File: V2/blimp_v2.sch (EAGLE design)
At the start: 10 parts

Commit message: upload the finished routing pcb design
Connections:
- net GND: no longer U$2.GND, U$2.GND3, U$4.GND, U$4.GND3
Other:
- moved on the sheet: JP1, JP2, JP3, JP4, JP5, JP6, JP7

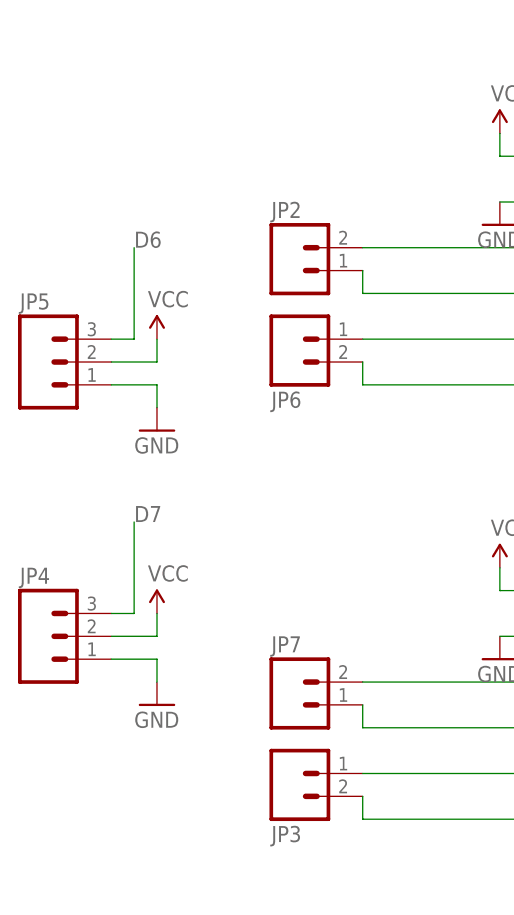
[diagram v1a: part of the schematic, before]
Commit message: add one more servo motor pinout
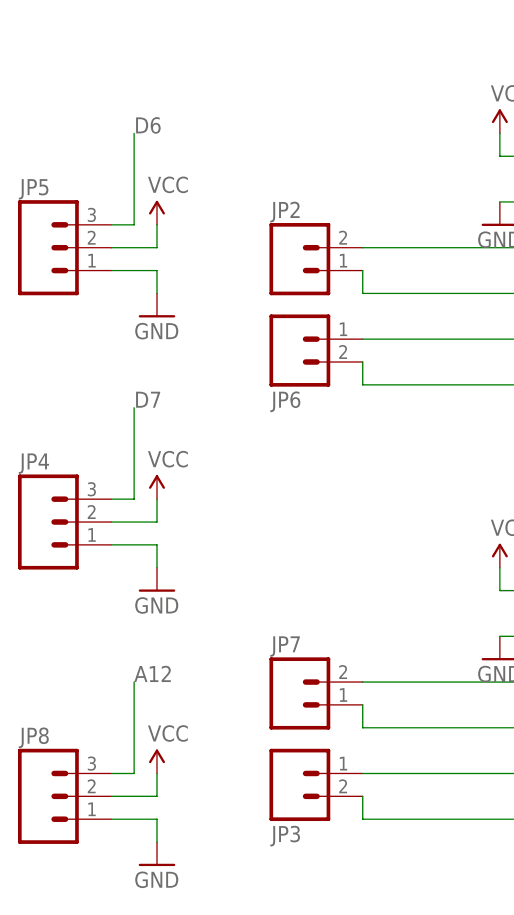
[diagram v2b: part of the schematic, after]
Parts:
- added JP8: (no value), SparkFun:M03PTH
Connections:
- net A12: now also JP8.3
- net GND: now also JP8.1
- net VCC: now also JP8.2
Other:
- moved on the sheet: JP4, JP5
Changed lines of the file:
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@@
 <part name="JP7" library="SparkFun" deviceset="M02" device="PTH"/>
 <part name="FRAME1" library="SparkFun-Aesthetics" library_urn="urn:adsk.eagle:library:507" deviceset="FRAME-A4L" device=""/>
+<part name="JP8" library="SparkFun" deviceset="M03" device="PTH"/>
+<part name="P+8" library="SparkFun" deviceset="VCC" device=""/>
+<part name="GND6" library="SparkFun" deviceset="GND" device=""/>
 </parts>
 <sheets>
@@
 <attribute name="NAME" x="-129.54" y="-41.402" size="1.778" layer="95" rot="MR180"/>
 </instance>
-<instance part="JP4" gate="G$1" x="-154.94" y="-20.32" smashed="yes">
-<attribute name="VALUE" x="-157.48" y="-27.94" size="1.778" layer="96"/>
-<attribute name="NAME" x="-157.48" y="-14.478" size="1.778" layer="95"/>
+<instance part="JP4" gate="G$1" x="-154.94" y="-7.62" smashed="yes">
+<attribute name="VALUE" x="-157.48" y="-15.24" size="1.778" layer="96"/>
+<attribute name="NAME" x="-157.48" y="-1.778" size="1.778" layer="95"/>
 </instance>
 <instance part="GND1" gate="1" x="35.56" y="7.62" smashed="yes">
@@
 <attribute name="VALUE" x="-106.68" y="-25.4" size="1.778" layer="96"/>
 </instance>
-<instance part="GND5" gate="1" x="-142.24" y="-27.94" smashed="yes">
-<attribute name="VALUE" x="-144.78" y="-30.48" size="1.778" layer="96"/>
-</instance>
-<instance part="P+4" gate="1" x="-142.24" y="-17.78" smashed="yes">
-<attribute name="VALUE" x="-143.256" y="-14.224" size="1.778" layer="96"/>
+<instance part="GND5" gate="1" x="-142.24" y="-15.24" smashed="yes">
+<attribute name="VALUE" x="-144.78" y="-17.78" size="1.778" layer="96"/>
+</instance>
+<instance part="P+4" gate="1" x="-142.24" y="-5.08" smashed="yes">
+<attribute name="VALUE" x="-143.256" y="-1.524" size="1.778" layer="96"/>
 </instance>
 <instance part="U$4" gate="G$1" x="-81.28" y="20.32" smashed="yes"/>
@@
 <attribute name="VALUE" x="-49.276" y="-19.304" size="1.778" layer="96"/>
 </instance>
-<instance part="JP5" gate="G$1" x="-154.94" y="10.16" smashed="yes">
-<attribute name="VALUE" x="-157.48" y="2.54" size="1.778" layer="96"/>
-<attribute name="NAME" x="-157.48" y="16.002" size="1.778" layer="95"/>
-</instance>
-<instance part="P+7" gate="1" x="-142.24" y="12.7" smashed="yes">
-<attribute name="VALUE" x="-143.256" y="16.256" size="1.778" layer="96"/>
-</instance>
-<instance part="GND8" gate="1" x="-142.24" y="2.54" smashed="yes">
-<attribute name="VALUE" x="-144.78" y="0" size="1.778" layer="96"/>
+<instance part="JP5" gate="G$1" x="-154.94" y="22.86" smashed="yes">
+<attribute name="VALUE" x="-157.48" y="15.24" size="1.778" layer="96"/>
+<attribute name="NAME" x="-157.48" y="28.702" size="1.778" layer="95"/>
+</instance>
+<instance part="P+7" gate="1" x="-142.24" y="25.4" smashed="yes">
+<attribute name="VALUE" x="-143.256" y="28.956" size="1.778" layer="96"/>
+</instance>
+<instance part="GND8" gate="1" x="-142.24" y="15.24" smashed="yes">
+<attribute name="VALUE" x="-144.78" y="12.7" size="1.778" layer="96"/>
 </instance>
 <instance part="JP6" gate="G$1" x="-127" y="12.7" smashed="yes" rot="MR180">
@@
 <attribute name="LAST_DATE_TIME" x="-6.35" y="-74.93" size="2.286" layer="94" font="vector"/>
 <attribute name="SHEET" x="7.62" y="-80.01" size="2.54" layer="94" font="vector"/>
+</instance>
+<instance part="JP8" gate="G$1" x="-154.94" y="-38.1" smashed="yes">
+<attribute name="VALUE" x="-157.48" y="-45.72" size="1.778" layer="96"/>
+<attribute name="NAME" x="-157.48" y="-32.258" size="1.778" layer="95"/>
+</instance>
+<instance part="P+8" gate="1" x="-142.24" y="-35.56" smashed="yes">
+<attribute name="VALUE" x="-143.256" y="-32.004" size="1.778" layer="96"/>
+</instance>
+<instance part="GND6" gate="1" x="-142.24" y="-45.72" smashed="yes">
+<attribute name="VALUE" x="-144.78" y="-48.26" size="1.778" layer="96"/>
 </instance>
 </instances>
@@
 <segment>
 <pinref part="JP4" gate="G$1" pin="1"/>
-<wire x1="-147.32" y1="-22.86" x2="-142.24" y2="-22.86" width="0.1524" layer="91"/>
-<wire x1="-142.24" y1="-22.86" x2="-142.24" y2="-25.4" width="0.1524" layer="91"/>
+<wire x1="-147.32" y1="-10.16" x2="-142.24" y2="-10.16" width="0.1524" layer="91"/>
+<wire x1="-142.24" y1="-10.16" x2="-142.24" y2="-12.7" width="0.1524" layer="91"/>
 <pinref part="GND5" gate="1" pin="GND"/>
 </segment>
@@
 <pinref part="JP5" gate="G$1" pin="1"/>
 <pinref part="GND8" gate="1" pin="GND"/>
-<wire x1="-147.32" y1="7.62" x2="-142.24" y2="7.62" width="0.1524" layer="91"/>
-<wire x1="-142.24" y1="7.62" x2="-142.24" y2="5.08" width="0.1524" layer="91"/>
+<wire x1="-147.32" y1="20.32" x2="-142.24" y2="20.32" width="0.1524" layer="91"/>
+<wire x1="-142.24" y1="20.32" x2="-142.24" y2="17.78" width="0.1524" layer="91"/>
+</segment>
+<segment>
+<pinref part="JP8" gate="G$1" pin="1"/>
+<pinref part="GND6" gate="1" pin="GND"/>
+<wire x1="-147.32" y1="-40.64" x2="-142.24" y2="-40.64" width="0.1524" layer="91"/>
+<wire x1="-142.24" y1="-40.64" x2="-142.24" y2="-43.18" width="0.1524" layer="91"/>
 </segment>
 </net>
@@
 <segment>
 <pinref part="JP4" gate="G$1" pin="2"/>
-<wire x1="-147.32" y1="-20.32" x2="-142.24" y2="-20.32" width="0.1524" layer="91"/>
-<wire x1="-142.24" y1="-20.32" x2="-142.24" y2="-17.78" width="0.1524" layer="91"/>
+<wire x1="-147.32" y1="-7.62" x2="-142.24" y2="-7.62" width="0.1524" layer="91"/>
+<wire x1="-142.24" y1="-7.62" x2="-142.24" y2="-5.08" width="0.1524" layer="91"/>
 <pinref part="P+4" gate="1" pin="VCC"/>
 </segment>
@@
 <pinref part="JP5" gate="G$1" pin="2"/>
 <pinref part="P+7" gate="1" pin="VCC"/>
-<wire x1="-147.32" y1="10.16" x2="-142.24" y2="10.16" width="0.1524" layer="91"/>
-<wire x1="-142.24" y1="10.16" x2="-142.24" y2="12.7" width="0.1524" layer="91"/>
+<wire x1="-147.32" y1="22.86" x2="-142.24" y2="22.86" width="0.1524" layer="91"/>
+<wire x1="-142.24" y1="22.86" x2="-142.24" y2="25.4" width="0.1524" layer="91"/>
+</segment>
+<segment>
+<pinref part="JP8" gate="G$1" pin="2"/>
+<pinref part="P+8" gate="1" pin="VCC"/>
+<wire x1="-147.32" y1="-38.1" x2="-142.24" y2="-38.1" width="0.1524" layer="91"/>
+<wire x1="-142.24" y1="-38.1" x2="-142.24" y2="-35.56" width="0.1524" layer="91"/>
 </segment>
 </net>
@@
 <segment>
 <pinref part="JP4" gate="G$1" pin="3"/>
-<wire x1="-147.32" y1="-17.78" x2="-144.78" y2="-17.78" width="0.1524" layer="91"/>
-<wire x1="-144.78" y1="-17.78" x2="-144.78" y2="-7.62" width="0.1524" layer="91"/>
-<label x="-144.78" y="-7.62" size="1.778" layer="95"/>
+<wire x1="-147.32" y1="-5.08" x2="-144.78" y2="-5.08" width="0.1524" layer="91"/>
+<wire x1="-144.78" y1="-5.08" x2="-144.78" y2="5.08" width="0.1524" layer="91"/>
+<label x="-144.78" y="5.08" size="1.778" layer="95"/>
 </segment>
 </net>
@@
 <segment>
 <pinref part="JP5" gate="G$1" pin="3"/>
-<wire x1="-147.32" y1="12.7" x2="-144.78" y2="12.7" width="0.1524" layer="91"/>
-<wire x1="-144.78" y1="12.7" x2="-144.78" y2="22.86" width="0.1524" layer="91"/>
-<label x="-144.78" y="22.86" size="1.778" layer="95"/>
+<wire x1="-147.32" y1="25.4" x2="-144.78" y2="25.4" width="0.1524" layer="91"/>
+<wire x1="-144.78" y1="25.4" x2="-144.78" y2="35.56" width="0.1524" layer="91"/>
+<label x="-144.78" y="35.56" size="1.778" layer="95"/>
 </segment>
 </net>
@@
 <label x="35.56" y="0" size="1.778" layer="95"/>
 </segment>
-</net>
+<segment>
+<pinref part="JP8" gate="G$1" pin="3"/>
+<wire x1="-147.32" y1="-35.56" x2="-144.78" y2="-35.56" width="0.1524" layer="91"/>
+<wire x1="-144.78" y1="-35.56" x2="-144.78" y2="-25.4" width="0.1524" layer="91"/>
+<label x="-144.78" y="-25.4" size="1.778" layer="95"/>
+</segment>
+</net>
